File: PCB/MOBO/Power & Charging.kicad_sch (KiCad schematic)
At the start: 46 parts, among them J201 USB_C_Receptacle_PowerOnly_6P, Q1 PMOS, Q2 NMOS, Q3 NMOS, Q4 NMOS, SW1 SW_DPST_x2, U1 BQ297xy, U2 AT90USB647-M, U202 MCP73871-1AA, U205 TPS61230DRC

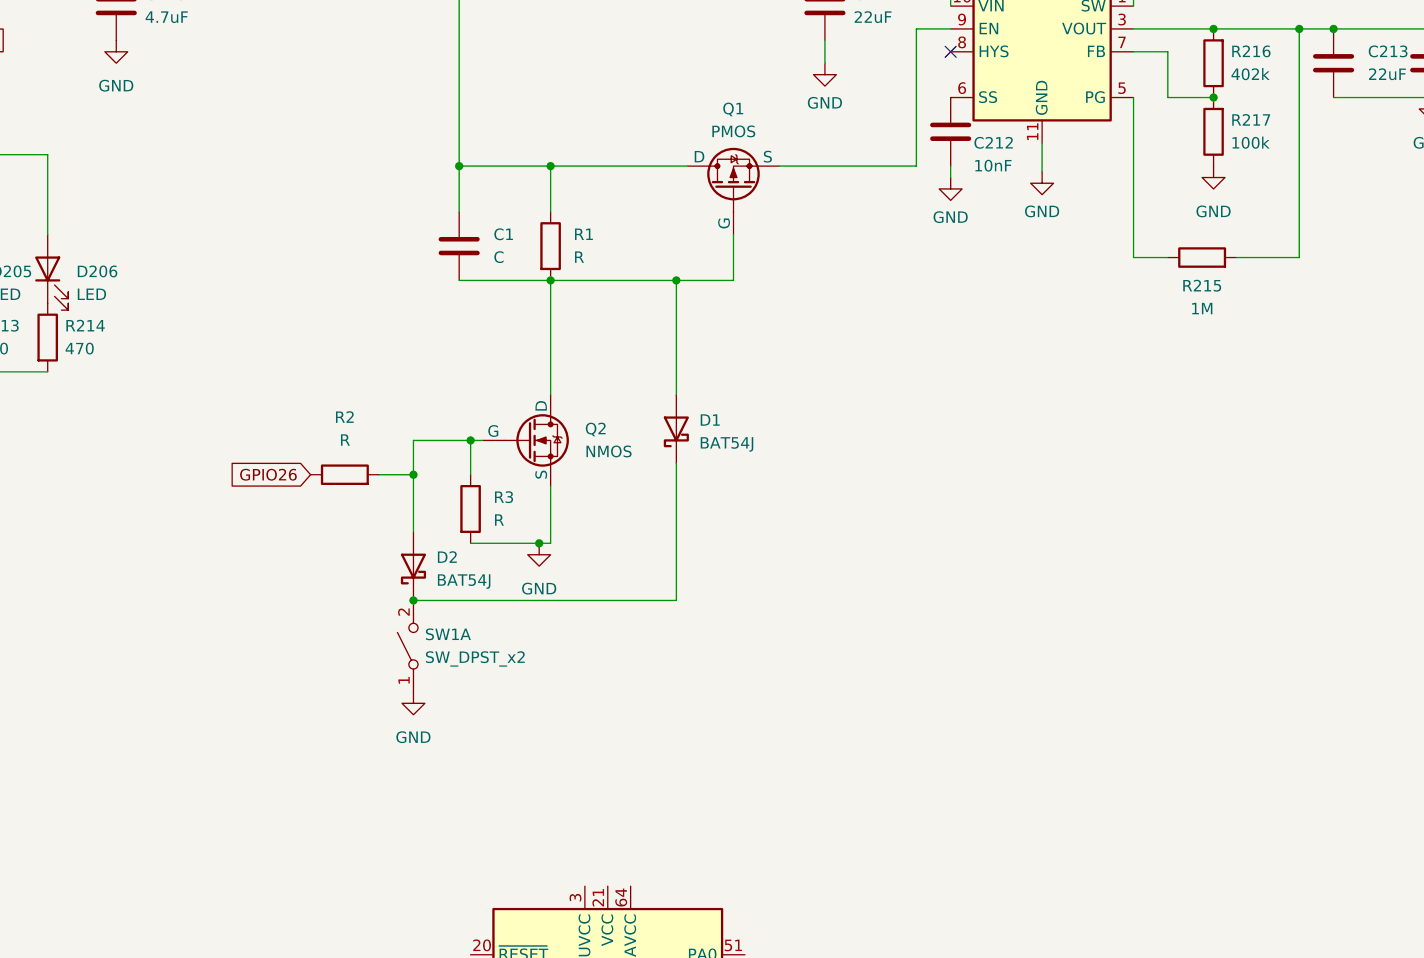
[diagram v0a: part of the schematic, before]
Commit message: fixed latch circuit lables
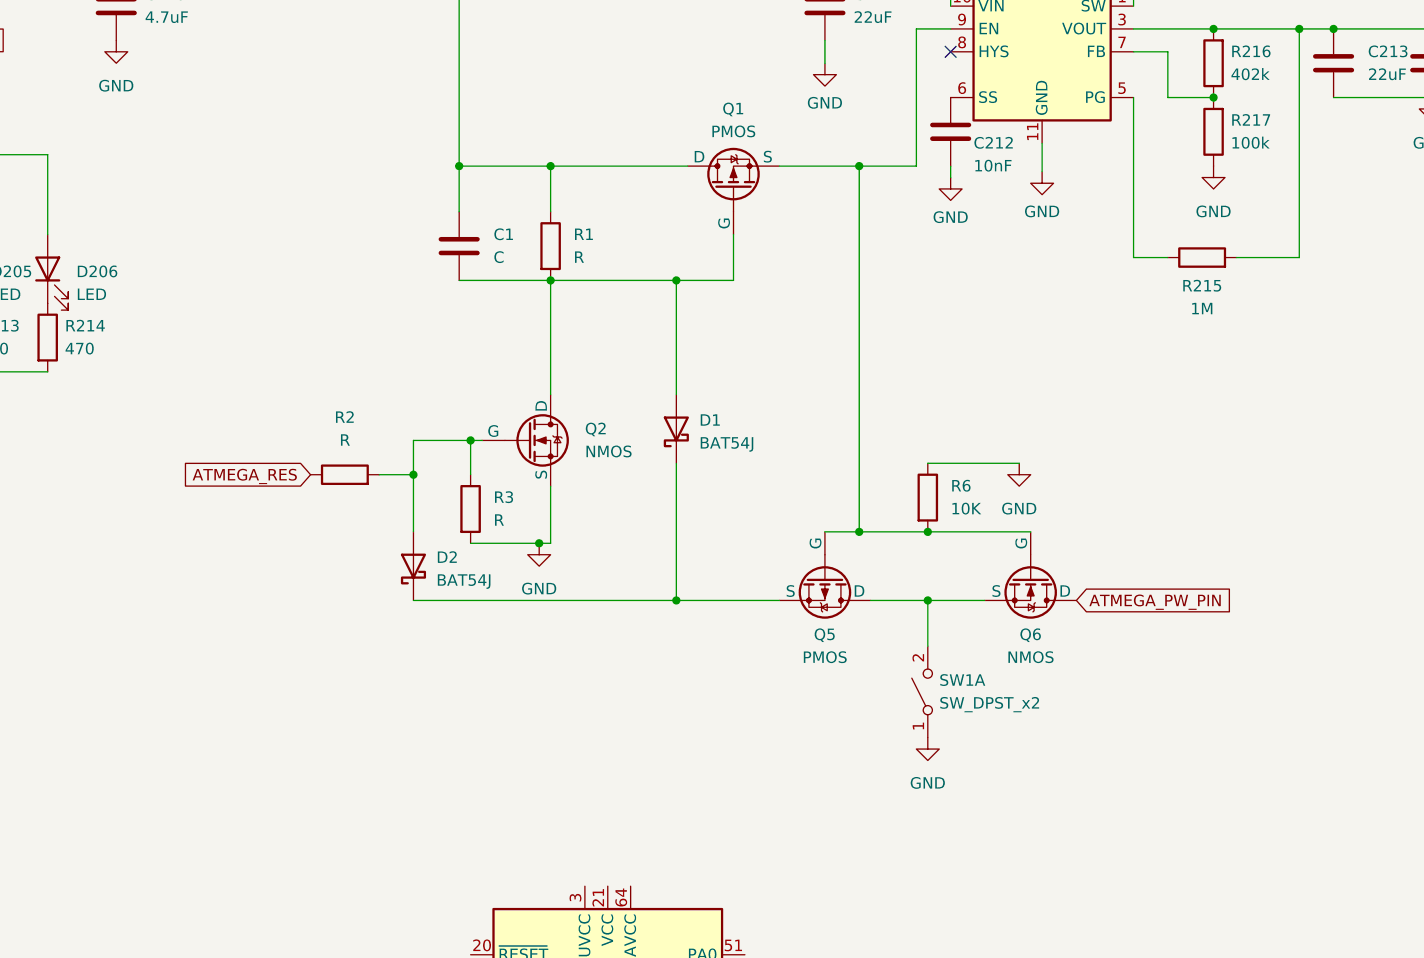
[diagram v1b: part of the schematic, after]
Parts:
- added Q5: PMOS, symbol Simulation_SPICE:PMOS
- added Q6: NMOS, symbol Simulation_SPICE:NMOS
- added R6: 10K, symbol Device:R
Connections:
- net GND: now also R6.1
- net at D1.1 (K), D2.1 (K): now also Q5.3 (S); no longer SW1.2 (B)
- net at Q1.3 (S), U205.9 (EN): now also Q5.2 (G), Q6.2 (G), R6.2
- net GPIO26 renamed ATMEGA_RES
- new net: Q5.1 (D), Q6.3 (S), SW1.2 (B)
- new net ATMEGA_PW_PIN: Q6.1 (D)
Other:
- moved on the sheet: SW1A

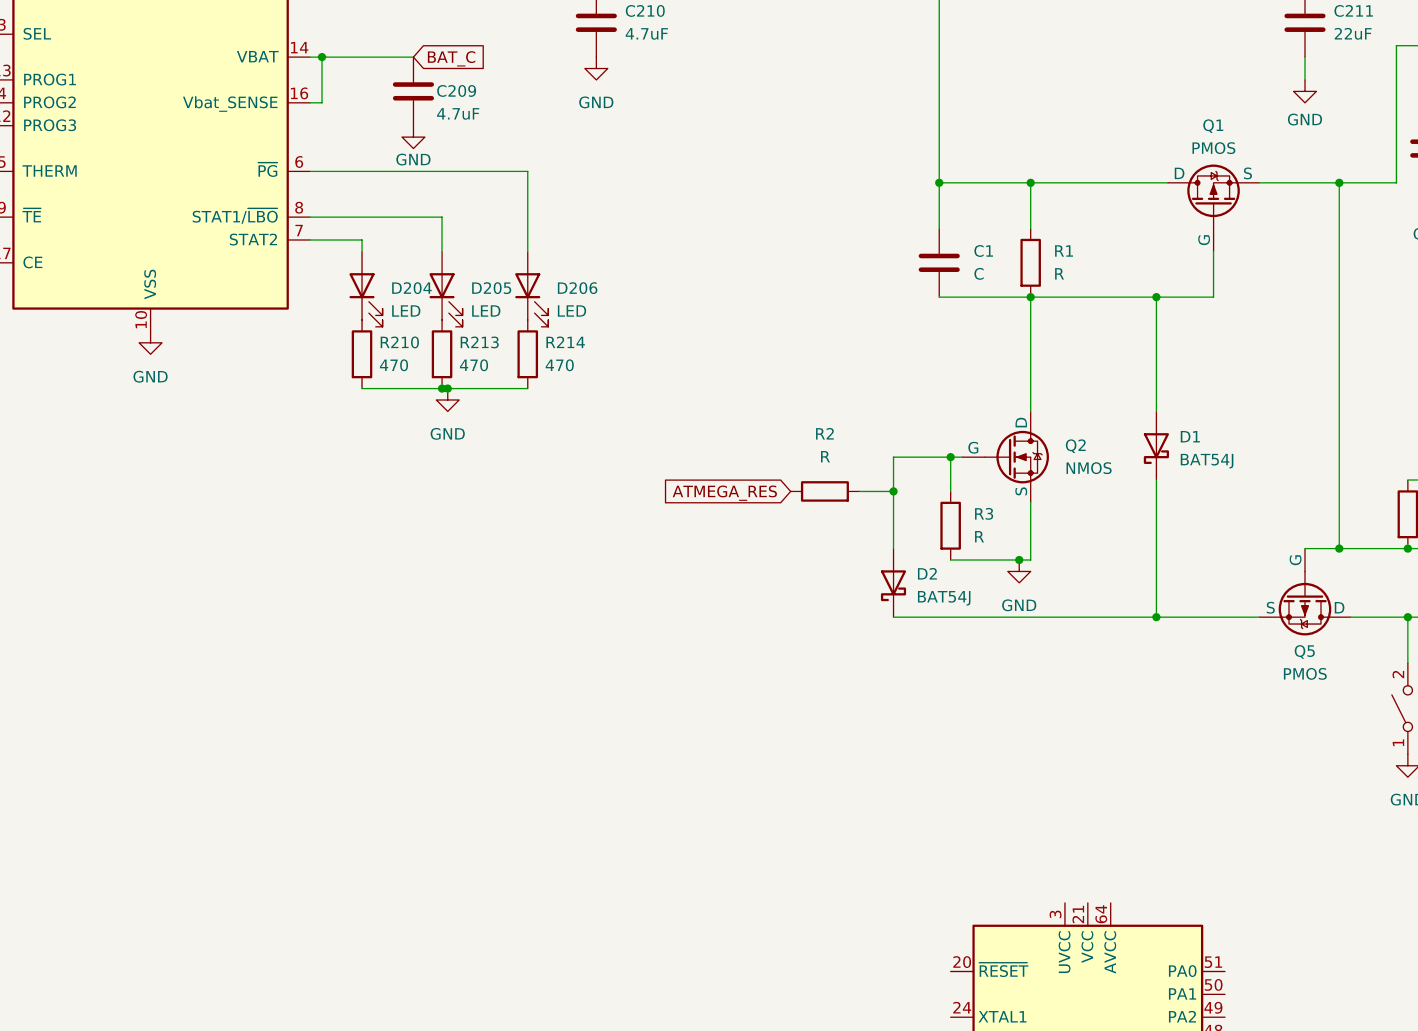
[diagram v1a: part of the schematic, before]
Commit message: Fixed resistor values for latch powering circuit
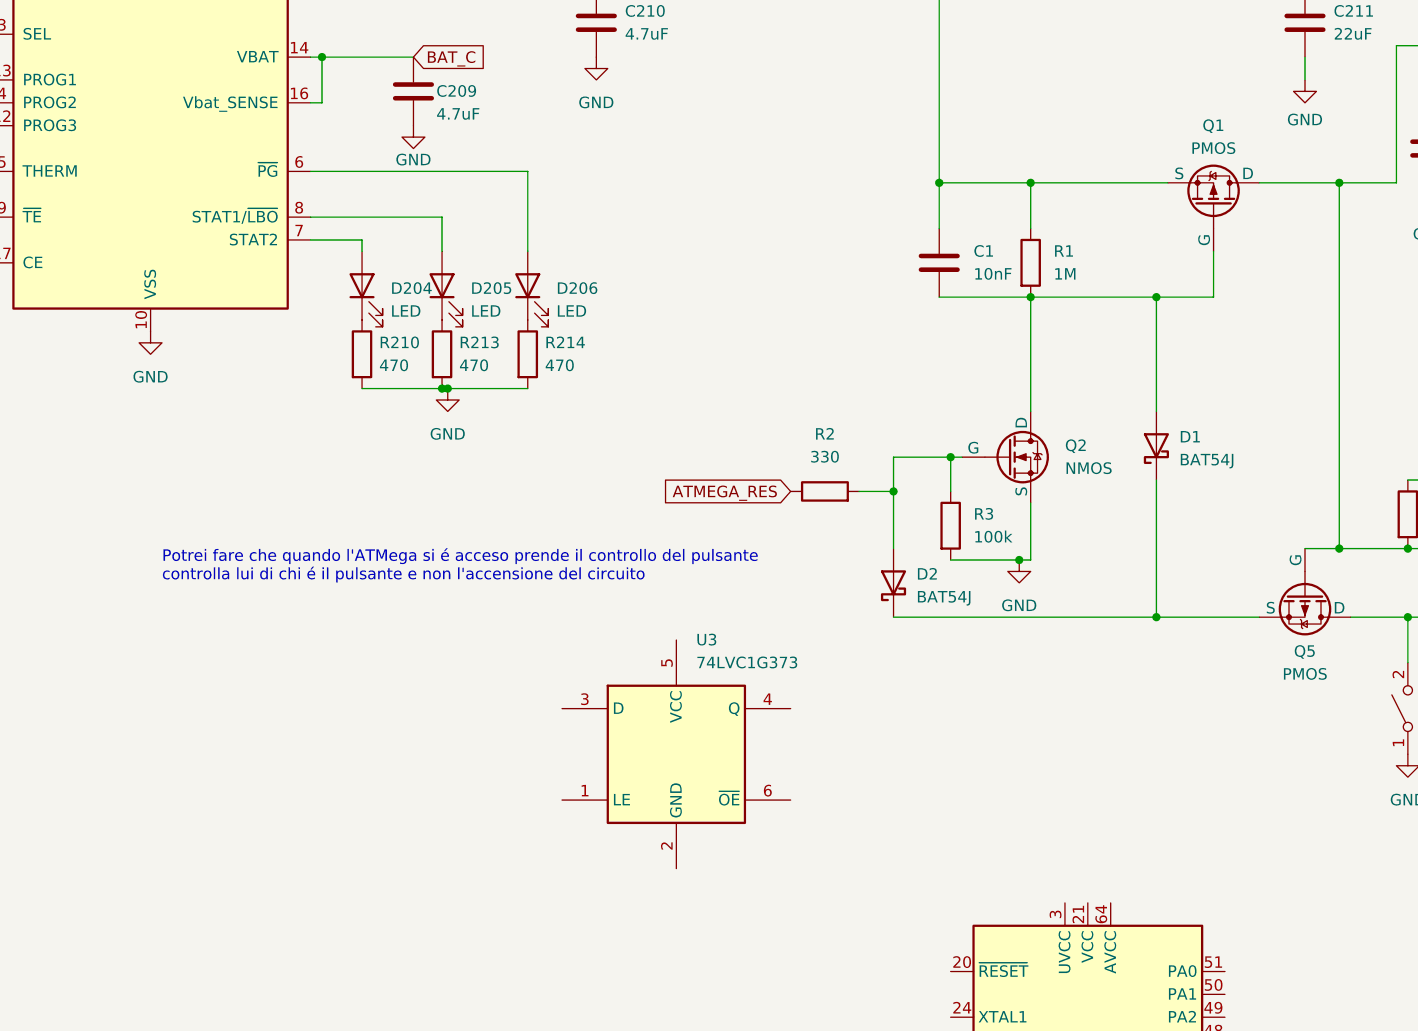
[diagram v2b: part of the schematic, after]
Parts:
- added U3: 74LVC1G373, symbol 74xGxx:74LVC1G373
- C1: value C -> 10nF
- R1: value R -> 1M
- R2: value R -> 330
- R3: value R -> 100k
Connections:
- net +3V8: now also Q1.3 (S); no longer Q1.1 (D)
- net at Q5.2 (G), Q6.2 (G), R6.2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: now also Q1.1 (D); no longer Q1.3 (S)
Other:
- note added: "Potrei fare che quando l'ATMega si é acceso prende il controllo del pulsante controlla lui di chi é il pulsante e non l'accensione del circuito"
- moved on the sheet: Q1
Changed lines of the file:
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@@
     (stroke (width 0) (type default))
+  )
+  (text "Potrei fare che quando l'ATMega si é acceso prende il controllo del pulsante\ncontrolla lui di chi é il pulsante e non l'accensione del circuito\n"
+    (at 156.21 102.87 0)
+    (effects (font (size 1.27 1.27)) (justify left bottom))
   )
   (global_label "BAT_C" (shape input) (at 184.15 44.45 0) (fields_autoplaced)
@@
       (effects (font (size 1.27 1.27)) (justify left))
     )
-    (property "Value" "R" (at 246.38 97.79 0)
+    (property "Value" "100k" (at 246.38 97.79 0)
       (effects (font (size 1.27 1.27)) (justify left))
     )
@@
       (effects (font (size 1.27 1.27)) (justify left))
     )
-    (property "Value" "R" (at 255.27 68.58 0)
+    (property "Value" "1M" (at 255.27 68.58 0)
       (effects (font (size 1.27 1.27)) (justify left))
     )
@@
     )
   )
+  (symbol (lib_id "74xGxx:74LVC1G373") (at 213.36 121.92 0) (unit 1)
+    (in_bom yes) (on_board yes) (dnp no) (fields_autoplaced)
+    (property "Reference" "U3" (at 215.5541 109.22 0)
+      (effects (font (size 1.27 1.27)) (justify left))
+    )
+    (property "Value" "74LVC1G373" (at 215.5541 111.76 0)
+      (effects (font (size 1.27 1.27)) (justify left))
+    )
+    (property "Footprint" "" (at 213.36 121.92 0)
+      (effects (font (size 1.27 1.27)) hide)
+    )
+    (property "Datasheet" "http://www.ti.com/lit/sg/scyt129e/scyt129e.pdf" (at 213.36 121.92 0)
+      (effects (font (size 1.27 1.27)) hide)
+    )
+    (pin "1")
+    (pin "2")
+    (pin "3")
+    (pin "4")
+    (pin "5")
+    (pin "6")
+    (instances
+      (project "MOBO"
+        (path "/2d62a3c1-c4f2-4921-9f6b-8dc8aef69d64/968b581c-59b8-4e39-ae9d-82f589704db7"
+          (reference "U3") (unit 1)
+        )
+      )
+    )
+  )
   (symbol (lib_id "Device:R") (at 113.03 33.02 0) (unit 1)
     (in_bom yes) (on_board yes) (dnp no) (fields_autoplaced)
@@
       (effects (font (size 1.27 1.27)) (justify left))
     )
-    (property "Value" "C" (at 246.38 68.58 0)
+    (property "Value" "10nF" (at 246.38 68.58 0)
       (effects (font (size 1.27 1.27)) (justify left))
     )
@@
     )
   )
-  (symbol (lib_id "Simulation_SPICE:PMOS") (at 273.05 60.96 90) (unit 1)
-    (in_bom yes) (on_board yes) (dnp no) (fields_autoplaced)
+  (symbol (lib_id "Simulation_SPICE:PMOS") (at 273.05 60.96 270) (mirror x) (unit 1)
+    (in_bom yes) (on_board yes) (dnp no)
     (property "Reference" "Q1" (at 273.05 52.07 90)
       (effects (font (size 1.27 1.27)))
@@
       (effects (font (size 1.27 1.27)))
     )
-    (property "Footprint" "" (at 270.51 55.88 0)
-      (effects (font (size 1.27 1.27)) hide)
-    )
-    (property "Datasheet" "https://ngspice.sourceforge.io/docs/ngspice-manual.pdf" (at 285.75 60.96 0)
-      (effects (font (size 1.27 1.27)) hide)
-    )
-    (property "Sim.Device" "PMOS" (at 290.195 60.96 0)
-      (effects (font (size 1.27 1.27)) hide)
-    )
-    (property "Sim.Type" "VDMOS" (at 292.1 60.96 0)
-      (effects (font (size 1.27 1.27)) hide)
-    )
-    (property "Sim.Pins" "1=D 2=G 3=S" (at 288.29 60.96 0)
+    (property "Footprint" "" (at 275.59 55.88 0)
+      (effects (font (size 1.27 1.27)) hide)
+    )
+    (property "Datasheet" "https://ngspice.sourceforge.io/docs/ngspice-manual.pdf" (at 260.35 60.96 0)
+      (effects (font (size 1.27 1.27)) hide)
+    )
+    (property "Sim.Device" "PMOS" (at 255.905 60.96 0)
+      (effects (font (size 1.27 1.27)) hide)
+    )
+    (property "Sim.Type" "VDMOS" (at 254 60.96 0)
+      (effects (font (size 1.27 1.27)) hide)
+    )
+    (property "Sim.Pins" "1=D 2=G 3=S" (at 257.81 60.96 0)
       (effects (font (size 1.27 1.27)) hide)
     )
@@
       (effects (font (size 1.27 1.27)))
     )
-    (property "Value" "R" (at 229.87 88.9 90)
-      (effects (font (size 1.27 1.27)))
-    )
+    (property "Value" "330" (at 229.87 88.9 90)
+      (effects (font (size 1.27 1.27)))
+    )

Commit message: Added README
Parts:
- added Q7: DMP3013SFV, Package_SON:Diodes_PowerDI3333-8, symbol Transistor_FET:DMP3013SFV
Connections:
- new net: Q7.1 (S), Q7.2 (S), Q7.3 (S)
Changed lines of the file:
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@@
+    )
+  )
+  (symbol (lib_id "Transistor_FET:DMP3013SFV") (at 224.79 73.66 0) (unit 1)
+    (in_bom yes) (on_board yes) (dnp no) (fields_autoplaced)
+    (property "Reference" "Q7" (at 231.14 72.39 0)
+      (effects (font (size 1.27 1.27)) (justify left))
+    )
+    (property "Value" "DMP3013SFV" (at 231.14 74.93 0)
+      (effects (font (size 1.27 1.27)) (justify left))
+    )
+    (property "Footprint" "Package_SON:Diodes_PowerDI3333-8" (at 229.87 75.565 0)
+      (effects (font (size 1.27 1.27) italic) (justify left) hide)
+    )
+    (property "Datasheet" "https://www.diodes.com/assets/Datasheets/DMP3013SFV.pdf" (at 224.79 73.66 90)
+      (effects (font (size 1.27 1.27)) (justify left) hide)
+    )
+    (pin "1")
+    (pin "2")
+    (pin "3")
+    (pin "4")
+    (pin "5")
+    (instances
+      (project "MOBO"
+        (path "/2d62a3c1-c4f2-4921-9f6b-8dc8aef69d64/968b581c-59b8-4e39-ae9d-82f589704db7"
+          (reference "Q7") (unit 1)
+        )
+      )
     )
   )
